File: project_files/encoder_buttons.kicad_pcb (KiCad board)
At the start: 2 copper layers, 63.5 x 25.4 mm, 40 parts, among them J1 UPPER, SW1 A, SW3 B, SW4 A, SW5 C, SW6 B, SW7 C, SW8 EC11, U1 74HC14, U2 74HC14

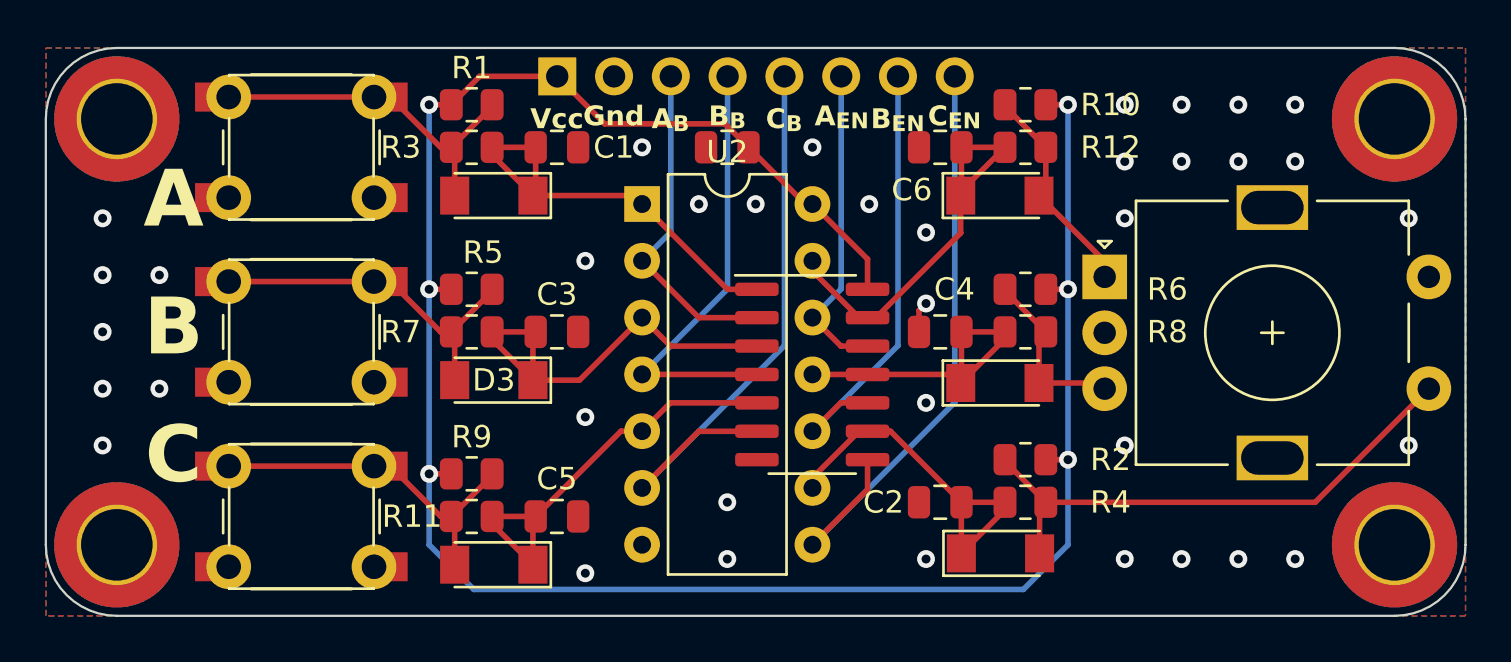
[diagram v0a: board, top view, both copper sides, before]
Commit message: Re-routed with wider traces
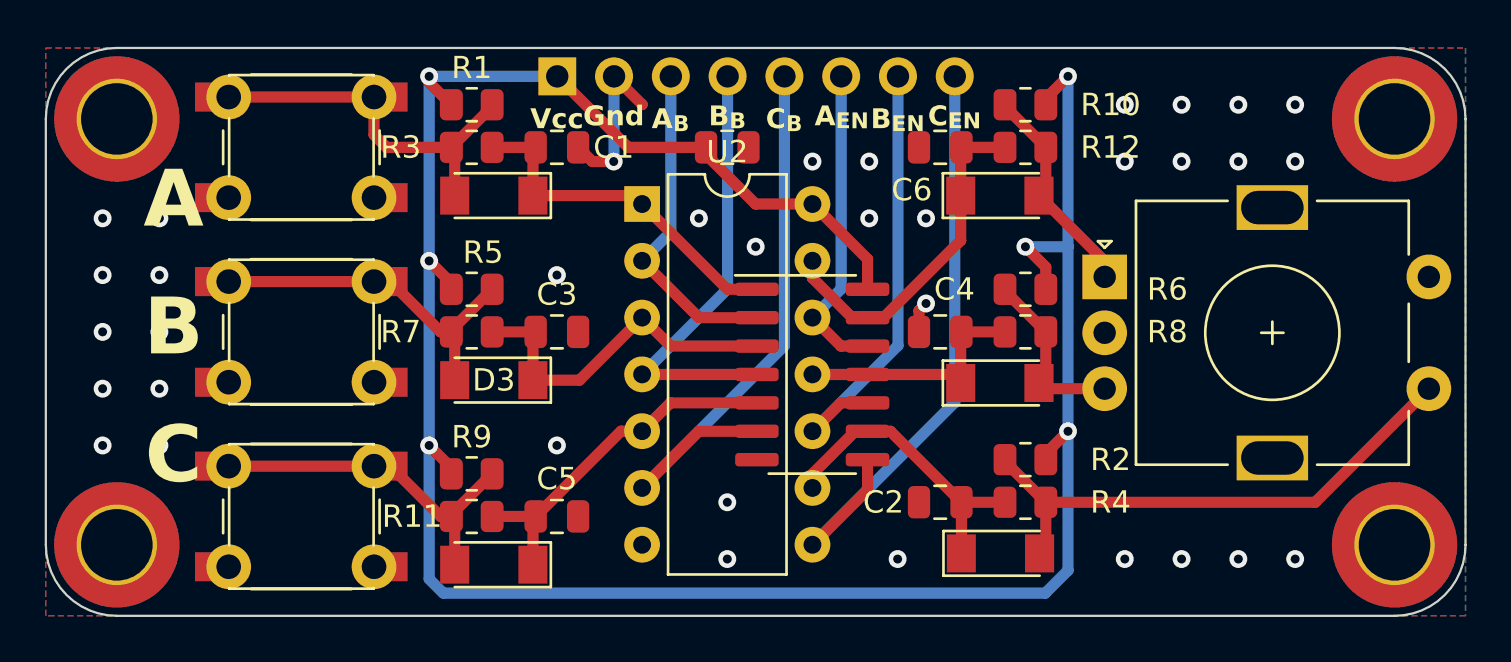
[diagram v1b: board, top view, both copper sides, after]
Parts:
- turned C7 to 0 degrees
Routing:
- net VCC: track 99.4 -> 111.1 mm
- net GND: track 1.40 -> 8.86 mm, vias 37 -> 35
- net /ENC_B: track 14.1 -> 11.0 mm
- net /ENC_C: track 16.6 -> 13.6 mm
- net /BUT_B: track 18.8 -> 15.9 mm
- net /BUT_A: track 18.8 -> 15.9 mm
- net /BUT_C: track 19.1 -> 16.2 mm
- net /ENC_A: track 18.3 -> 15.7 mm
- net Net-(D1-A): track 15.0 -> 16.8 mm
- net Net-(D3-A): track 15.8 -> 15.0 mm
